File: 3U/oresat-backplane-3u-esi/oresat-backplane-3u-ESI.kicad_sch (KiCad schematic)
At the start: 12 parts

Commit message: Added schematic and board variables, polished some silkscreen, reviewed board, renamed directory
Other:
- company: Portland State Aerospace Society -> PSAS / ESI
- title: Generic OreSat 3U Backplane -> OreSat 3U Backplane for ESI
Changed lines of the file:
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@@
 	(paper "B")
 	(title_block
-		(title "Generic OreSat 3U Backplane")
-		(date "2025-10-21")
+		(title "OreSat 3U Backplane for ESI")
+		(date "2026-02-20")
 		(rev "1.0")
-		(company "Portland State Aerospace Society")
+		(company "PSAS / ESI")
 	)
 	(wire

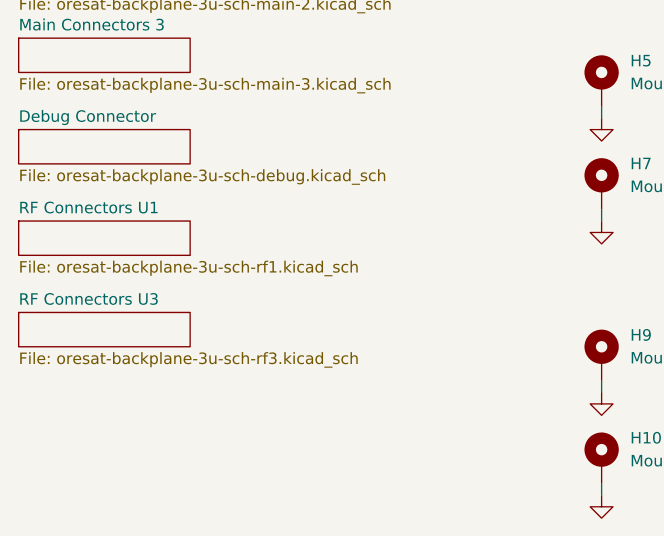
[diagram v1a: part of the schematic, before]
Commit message: Labelled connectors & disconnected C3 LBand
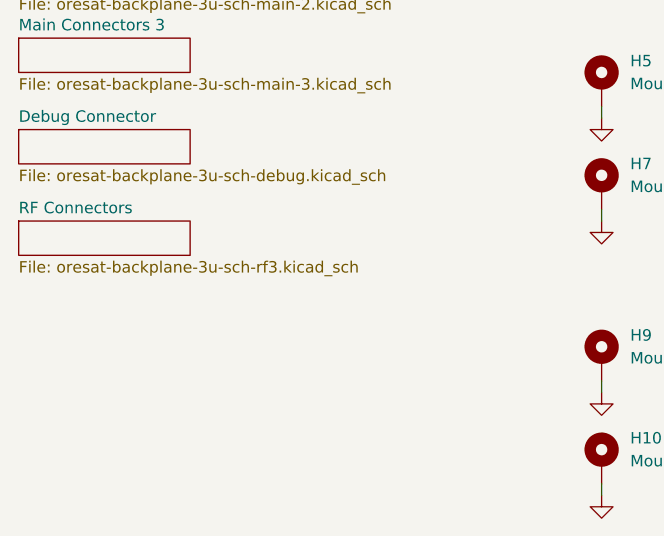
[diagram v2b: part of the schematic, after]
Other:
- sheet RF Connectors U3 renamed RF Connectors
- removed sheet RF Connectors U1
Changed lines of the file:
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@@
 			(project "oresat-backplane-3u-ESI"
 				(path "/300eeac4-6caf-4310-939c-5dc51539800c"
-					(page "7")
+					(page "5")
 				)
 			)
@@
 				(path "/300eeac4-6caf-4310-939c-5dc51539800c"
 					(page "2")
-				)
-			)
-		)
-	)
-	(sheet
-		(at 68.58 133.35)
-		(size 19.05 3.81)
-		(exclude_from_sim no)
-		(in_bom yes)
-		(on_board yes)
-		(dnp no)
-		(fields_autoplaced yes)
-		(stroke
-			(width 0.1524)
-			(type solid)
-		)
-		(fill
-			(color 0 0 0 0.0000)
-		)
-		(property "Sheetname" "RF Connectors U1"
-			(at 68.58 132.6384 0)
-			(effects
-				(font
-					(size 1.27 1.27)
-				)
-				(justify left bottom)
-			)
-		)
-		(property "Sheetfile" "oresat-backplane-3u-sch-rf1.kicad_sch"
-			(at 68.58 137.7446 0)
-			(effects
-				(font
-					(size 1.27 1.27)
-				)
-				(justify left top)
-			)
-		)
-		(property "Field2" ""
-			(at 68.58 133.35 0)
-			(effects
-				(font
-					(size 1.27 1.27)
-				)
-			)
-		)
-		(property "Field3" ""
-			(at 68.58 133.35 0)
-			(effects
-				(font
-					(size 1.27 1.27)
-				)
-			)
-		)
-		(instances
-			(project "oresat-backplane-3u-ESI"
-				(path "/300eeac4-6caf-4310-939c-5dc51539800c"
-					(page "8")
 				)
 			)
@@
 	)
 	(sheet
-		(at 68.58 143.51)
+		(at 68.58 133.35)
 		(size 19.05 3.81)
 		(exclude_from_sim no)
@@
 			(color 0 0 0 0.0000)
 		)
-		(property "Sheetname" "RF Connectors U3"
-			(at 68.58 142.7984 0)
+		(property "Sheetname" "RF Connectors"
+			(at 68.58 132.6384 0)
 			(effects
 				(font
@@
 		)
 		(property "Sheetfile" "oresat-backplane-3u-sch-rf3.kicad_sch"
-			(at 68.58 147.9046 0)
+			(at 68.58 137.7446 0)
 			(effects
 				(font
@@
 			(project "oresat-backplane-3u-ESI"
 				(path "/300eeac4-6caf-4310-939c-5dc51539800c"
-					(page "10")
+					(page "6")
 				)
 			)
